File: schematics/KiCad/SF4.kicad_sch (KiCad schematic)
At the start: 31 parts, among them J1 Power, J2 Digital/PWM, J3 Analog, J4 Digital/PWM, J5 AudioJack2, J6 AudioJack2, U1 TL072, U2 LM358, U3 MCP6002-xP, U6 VTL5C

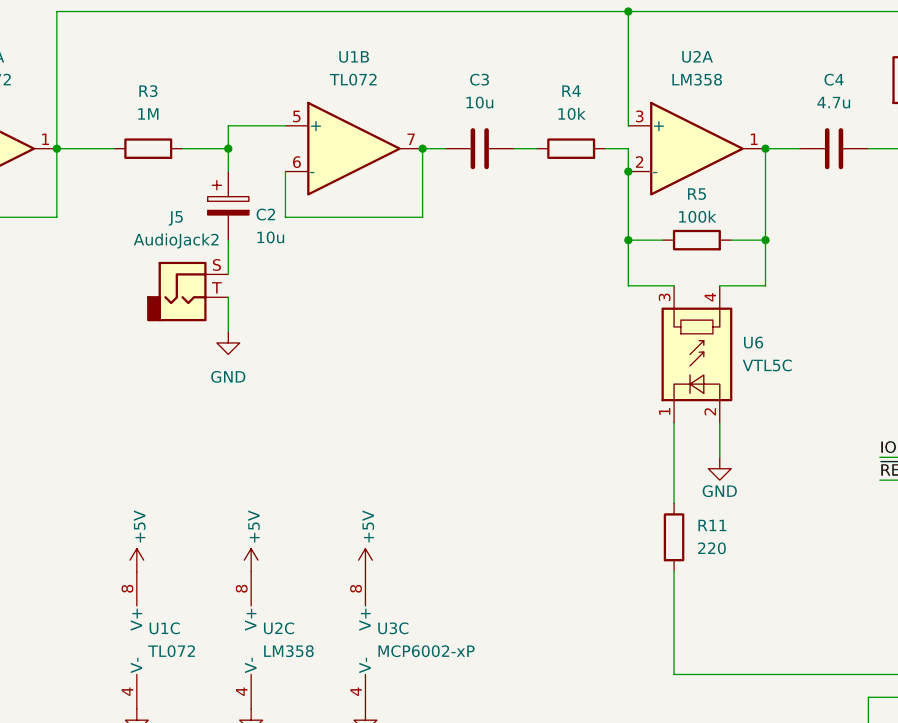
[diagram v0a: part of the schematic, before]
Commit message: Optocoupler performance tested
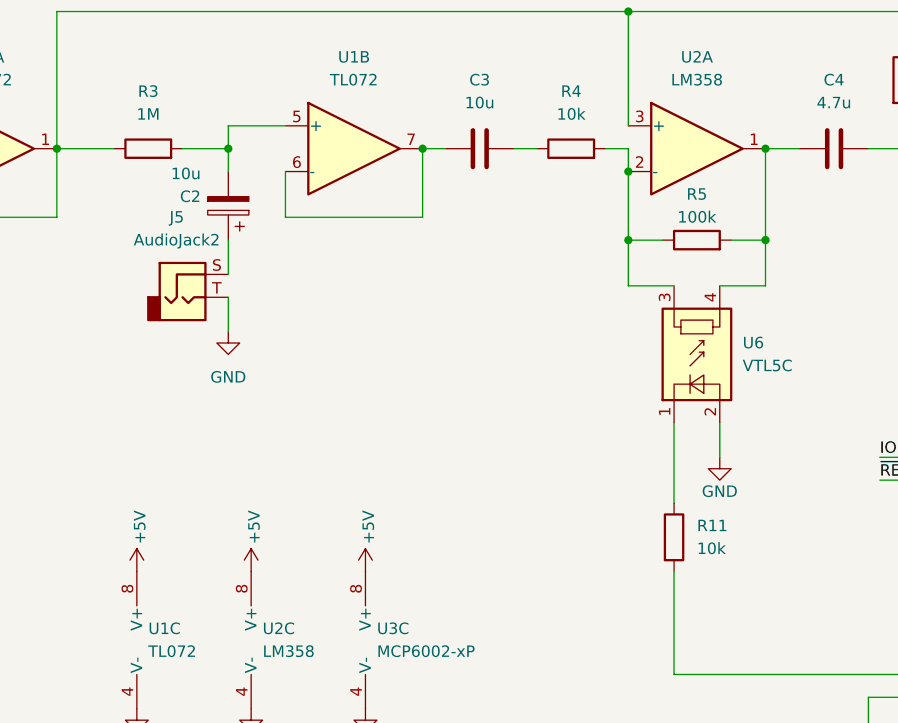
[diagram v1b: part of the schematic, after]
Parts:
- R11: value 220 -> 10k
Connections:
- net at R3.2, U1.5 (+): now also C2.2; no longer C2.1
- net at J5.S: now also C2.1; no longer C2.2
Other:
- moved on the sheet: C2
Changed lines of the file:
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@@
 	)
 	(junction
-		(at 86.36 60.96)
-		(diameter 0)
-		(color 0 0 0 0)
-	)
-	(junction
 		(at 44.45 58.42)
 		(diameter 0)
@@
 	)
 	(junction
+		(at 86.36 60.96)
+		(diameter 0)
+		(color 0 0 0 0)
+	)
+	(junction
 		(at 196.85 60.96)
 		(diameter 0)
@@
 	(wire
 		(pts
+			(xy 86.36 71.12) (xy 86.36 74.93)
+		)
+		(stroke
+			(width 0)
+			(type default)
+		)
+	)
+	(wire
+		(pts
 			(xy 157.48 60.96) (xy 161.29 60.96)
 		)
@@
 	(wire
 		(pts
-			(xy 86.36 71.12) (xy 86.36 74.93)
-		)
-		(stroke
-			(width 0)
-			(type default)
-		)
-	)
-	(wire
-		(pts
 			(xy 223.52 139.7) (xy 223.52 129.54)
 		)
@@
 	(wire
 		(pts
-			(xy 86.36 60.96) (xy 86.36 63.5)
+			(xy 223.52 147.32) (xy 223.52 149.86)
 		)
 		(stroke
@@
 	(wire
 		(pts
-			(xy 223.52 147.32) (xy 223.52 149.86)
+			(xy 86.36 58.42) (xy 86.36 60.96)
 		)
 		(stroke
@@
 	(wire
 		(pts
-			(xy 86.36 58.42) (xy 86.36 60.96)
+			(xy 86.36 60.96) (xy 86.36 63.5)
 		)
 		(stroke
@@
 	(symbol
 		(lib_id "Device:C_Polarized")
-		(at 86.36 67.31 0)
+		(at 86.36 67.31 180)
 		(unit 1)
 		(body_style 1)
@@
 		(dnp no)
 		(property "Reference" "C2"
-			(at 89.408 68.326 0)
+			(at 83.312 66.294 0)
 			(show_name no)
 			(do_not_autoplace no)
@@
 		)
 		(property "Value" "10u"
-			(at 89.408 70.866 0)
+			(at 83.312 63.754 0)
 			(show_name no)
 			(do_not_autoplace no)
@@
 		)
 		(property "Footprint" ""
-			(at 87.3252 71.12 0)
+			(at 85.3948 63.5 0)
 			(hide yes)
 			(show_name no)
@@
 			)
 		)
-		(property "Value" "220"
+		(property "Value" "10k"
 			(at 138.43 105.4099 0)
 			(show_name no)
